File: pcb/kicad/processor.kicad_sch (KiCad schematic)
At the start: 1 part, among them U3 STM32F401RBTx

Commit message: Move USB to own sheet.
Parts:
- added C4 (x5): 100n, Capacitor_SMD:C_0805_2012Metric, symbol Device:C
- added C4 (x2): 4.7u, Capacitor_SMD:C_0805_2012Metric, symbol Device:C
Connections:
- net VDD: now reaches U3.1 (VBAT)
- net VDD: now also U3.19 (VDD), U3.32 (VDD), U3.48 (VDD), U3.64 (VDD), C4.1, C4.1, C4.1, C4.1, C4.1, C4.1
- net VCAP: now reaches U3.30 (VCAP1)
- net VCAP: now also C4.1
- new net GND: C4.2, C4.2, C4.2, C4.2, C4.2, C4.2, C4.2
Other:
- moved on the sheet: U3

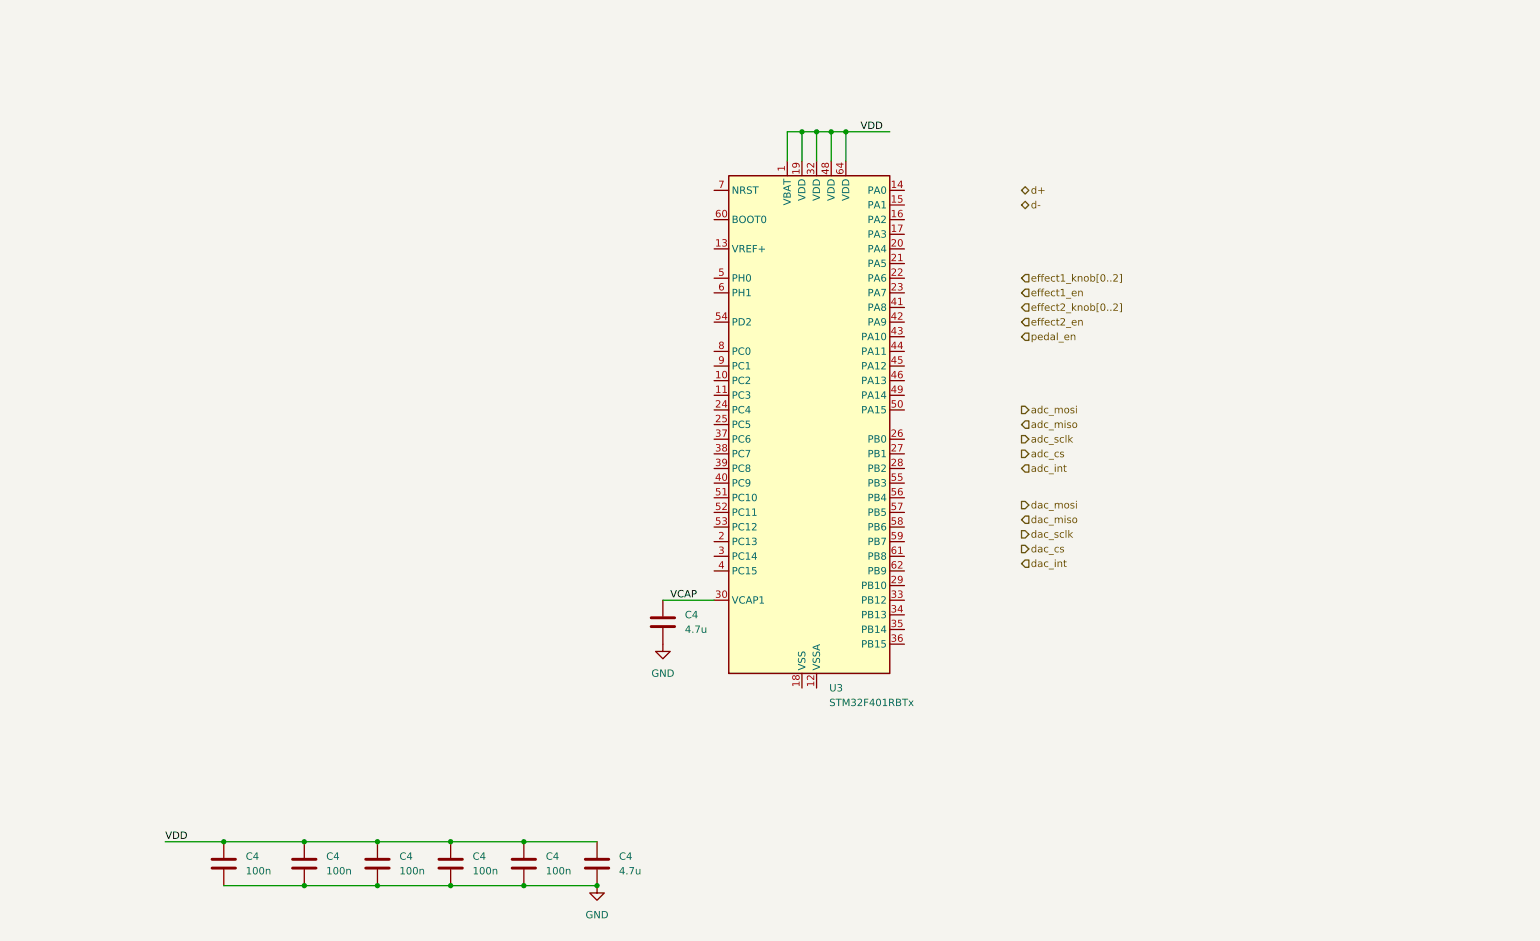
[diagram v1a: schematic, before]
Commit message: Add SoC and pinout.
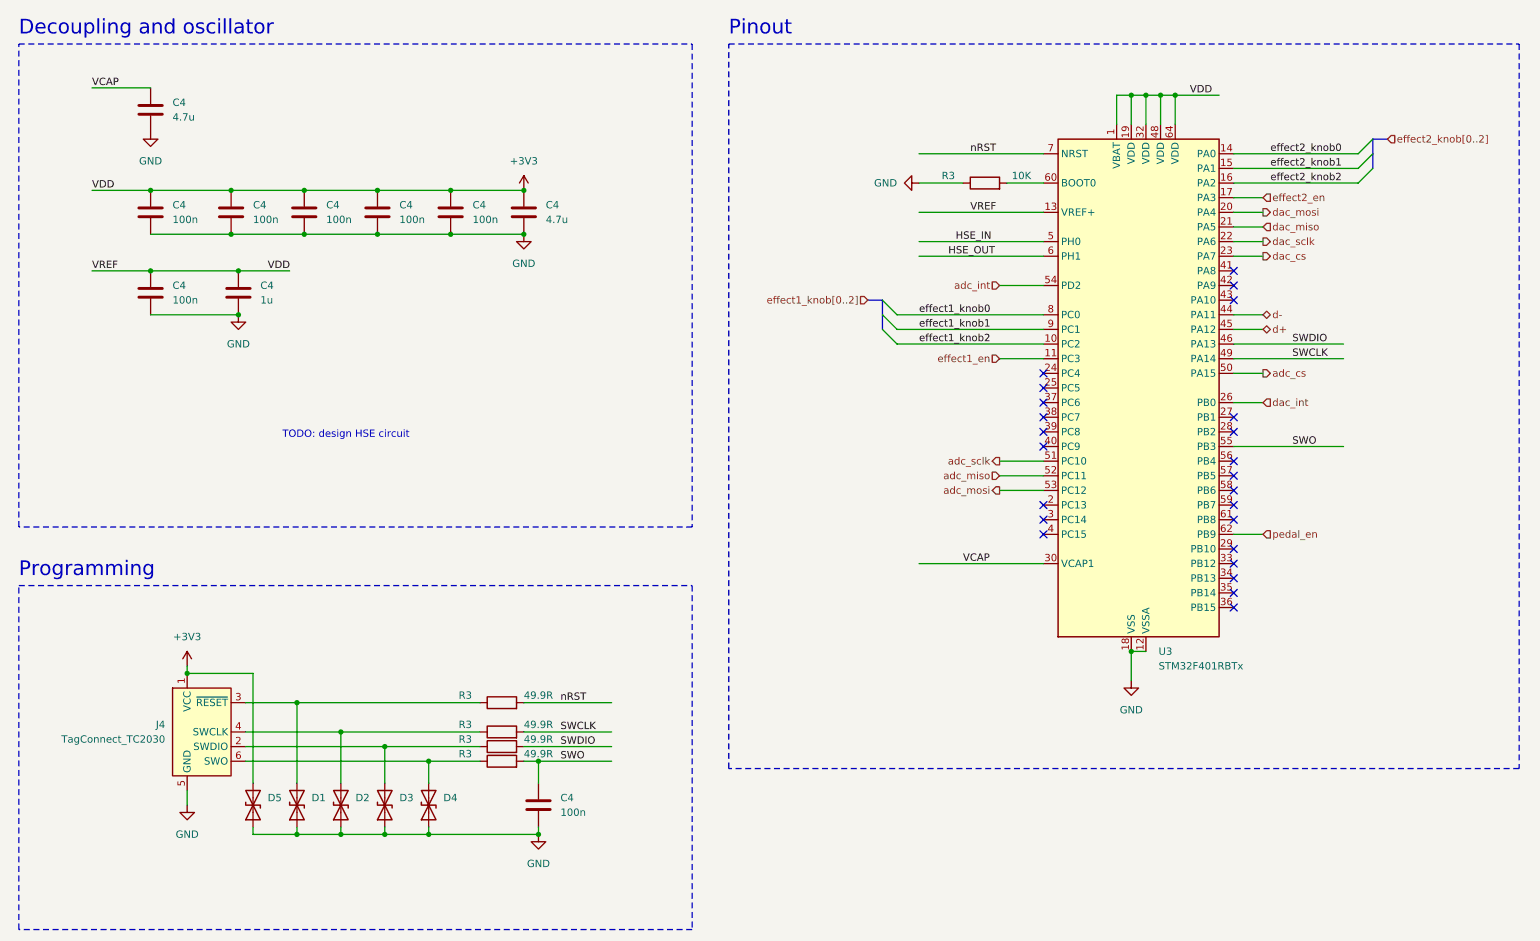
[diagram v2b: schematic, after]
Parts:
- removed C4: 4.7u, Capacitor_SMD:C_0805_2012Metric, symbol Device:C
- added C4: 1u, Capacitor_SMD:C_0805_2012Metric, symbol Device:C
- added C4 (x2): 100n, Capacitor_SMD:C_0805_2012Metric, symbol Device:C
- added C4: 4.7u, Capacitor_SMD:C_0805_2012Metric, symbol Device:C
- added D1, D2, D3, D4, D5: D_TVS, symbol Device:D_TVS
- added J4: TagConnect_TC2030, Connector:Tag-Connect_TC2030-IDC-FP_2x03_P1.27mm_Vertical, symbol Connector:Conn_ARM_SWD_TagConnect_TC2030
- added R3 (x4): 49.9R, Resistor_SMD:R_0805_2012Metric, symbol Device:R
- added R3: 10K, Resistor_SMD:R_0805_2012Metric, symbol Device:R
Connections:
- net VDD is gone; now on net +3V3: C4.1, C4.1, C4.1, C4.1, C4.1, C4.1, U3.1 (VBAT), U3.19 (VDD), U3.32 (VDD), U3.48 (VDD), U3.64 (VDD)
- net GND: now also U3.12 (VSSA), U3.18 (VSS), U3.31 (VSS), U3.47 (VSS), U3.63 (VSS), C4.2, C4.2, C4.2, C4.2, D1.1 (A1), D2.1 (A1), D3.1 (A1), D4.1 (A1), D5.1 (A1), J4.5 (GND), R3.1
- net VCAP: now also C4.1
- net adc_cs: now also U3.50 (PA15)
- net adc_int: now also U3.54 (PD2)
- net adc_miso: now also U3.52 (PC11)
- net adc_mosi: now also U3.53 (PC12)
- net adc_sclk: now also U3.51 (PC10)
- net d+: now also U3.45 (PA12)
- net d-: now also U3.44 (PA11)
- net dac_cs: now also U3.23 (PA7)
- net dac_int: now also U3.26 (PB0)
- net dac_miso: now also U3.21 (PA5)
- net dac_mosi: now also U3.20 (PA4)
- net dac_sclk: now also U3.22 (PA6)
- net effect1_en: now also U3.11 (PC3)
- net effect2_en: now also U3.17 (PA3)
- net pedal_en: now also U3.62 (PB9)
- net effect1_knob2: now reaches U3.10 (PC2)
- net +3V3: now reaches U3.13 (VREF+)
- net +3V3: now also C4.1, C4.1, D5.2 (A2), J4.1 (VCC)
- net effect2_knob0: now reaches U3.14 (PA0)
- net effect2_knob1: now reaches U3.15 (PA1)
- net effect2_knob2: now reaches U3.16 (PA2)
- net SWDIO: now reaches U3.46 (PA13)
- net SWDIO: now also R3.2
- net SWCLK: now reaches U3.49 (PA14)
- net SWCLK: now also R3.2
- net HSE_IN: now reaches U3.5 (PH0)
- net SWO: now reaches U3.55 (PB3)
- net SWO: now also C4.1, R3.2
- net HSE_OUT: now reaches U3.6 (PH1)
- net at U3.60 (BOOT0): now also R3.2
- net nRST: now reaches U3.7 (NRST)
- net nRST: now also R3.2
- net effect1_knob0: now reaches U3.8 (PC0)
- net effect1_knob1: now reaches U3.9 (PC1)
- new net: D4.2 (A2), J4.6 (SWO), R3.1
- new net: D3.2 (A2), J4.2 (SWDIO), R3.1
- new net: D1.2 (A2), J4.3 (~{RESET}), R3.1
- new net: D2.2 (A2), J4.4 (SWCLK), R3.1
- no-connect marks 0 -> 24
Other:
- note added: "Decoupling and oscillator"
- note added: "Pinout"
- note added: "Programming"
- note added: "TODO: design HSE circuit"
- moved on the sheet: C4, U3

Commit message: Add hse circuit.
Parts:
- added C4 (x2): 10p, Capacitor_SMD:C_0805_2012Metric, symbol Device:C
- added R3: 0R, Resistor_SMD:R_0805_2012Metric, symbol Device:R
- added Y1: 16MHz, symbol Device:Crystal_GND24
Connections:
- net GND: now also C4.2, C4.2, Y1.2, Y1.4
- net HSE_IN: now also C4.1, Y1.1
- net HSE_OUT: now also R3.2
- new net: C4.1, R3.1, Y1.3
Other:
- note added: "For RH100-16.000-8-2020-TR, C_0 = 8pF and ESR = 70R. Considering stray capacitance of 3 to 5pF, C_L = 2 * (C_0 - C_S) = 6 to 10pF."
- note removed: "TODO: design HSE circuit"

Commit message: Added converters, controls and updated annotations.
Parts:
- removed D1, D2, D3, D4, D5: D_TVS, symbol Device:D_TVS
- added D301, D302, D303, D304, D305: ~, symbol pedal-components:PESD3V3L1BA
- renumbered J4 to J301, U3 to U301, Y1 to Y301
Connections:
- net +3V3: now also D301.2 (A2)
- net GND: now also D301.1 (A1), D302.1 (A1), D303.1 (A1), D304.1 (A1), D305.1 (A1)
- net SWO: no longer C4.1
- net nRST: now also C4.1
- net DAC_NLDAC: now reaches U301.41 (PA8)
- net DAC_NCLR: now reaches U301.42 (PA9)
- net at J301.6 (SWO), R3.1: now also D305.2 (A2)
- net at J301.2 (SWDIO), R3.1: now also D304.2 (A2)
- net at J301.3 (~{RESET}), R3.1: now also D302.2 (A2)
- net at J301.4 (SWCLK), R3.1: now also D303.2 (A2)
- net adc_cs renamed ADC_NCS
- net adc_int: no longer names the net of U301.54 (PD2)
- net adc_miso renamed ADC_MISO
- net adc_mosi: no longer names the net of U301.53 (PC12)
- net adc_sclk renamed ADC_SCLK
- net d+ renamed D+
- net d- renamed D-
- net dac_cs renamed DAC_CS
- net dac_int: no longer names the net of U301.26 (PB0)
- net dac_miso: no longer names the net of U301.21 (PA5)
- net dac_mosi renamed DAC_MOSI
- net dac_sclk renamed DAC_SCLK
- net effect1_en renamed EFFECT1_EN
- net effect1_knob0 renamed EFFECT1_KNOB0
- net effect1_knob1 renamed EFFECT1_KNOB1
- net effect1_knob2 renamed EFFECT1_KNOB2
- net effect2_en renamed EFFECT2_EN
- net effect2_knob0 renamed EFFECT2_KNOB0
- net effect2_knob1 renamed EFFECT2_KNOB1
- net effect2_knob2 renamed EFFECT2_KNOB2
- net pedal_en renamed PEDAL_EN
- no-connect marks 24 -> 26
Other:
- moved on the sheet: C4, J301, R3

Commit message: Added PCB layout and fabrication output.
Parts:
- D301, D302, D303, D304, D305: footprint (none) -> pedal-components:PESD3V3L1BA
- Y301: footprint (none) -> pedal-components:RH100-16.000-8-2020-TR; Part Number (none) -> RH100-16.000-8-2020-TR; Part number RH100-16.000-8-2020-TR -> (none)
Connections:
- net TAG_SWO: now reaches D305.2 (A2), J301.6 (SWO), R3.1
- net HSE_PRE_OUT: now reaches C4.1, R3.1, Y301.3
- net TAG_SWDIO: now reaches D304.2 (A2), J301.2 (SWDIO), R3.1
- net BOOT0: now reaches R3.2, U301.60 (BOOT0)
- net TAG_nRST: now reaches D302.2 (A2), J301.3 (~{RESET}), R3.1
- net TAG_SWCLK: now reaches D303.2 (A2), J301.4 (SWCLK), R3.1
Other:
- moved on the sheet: R3

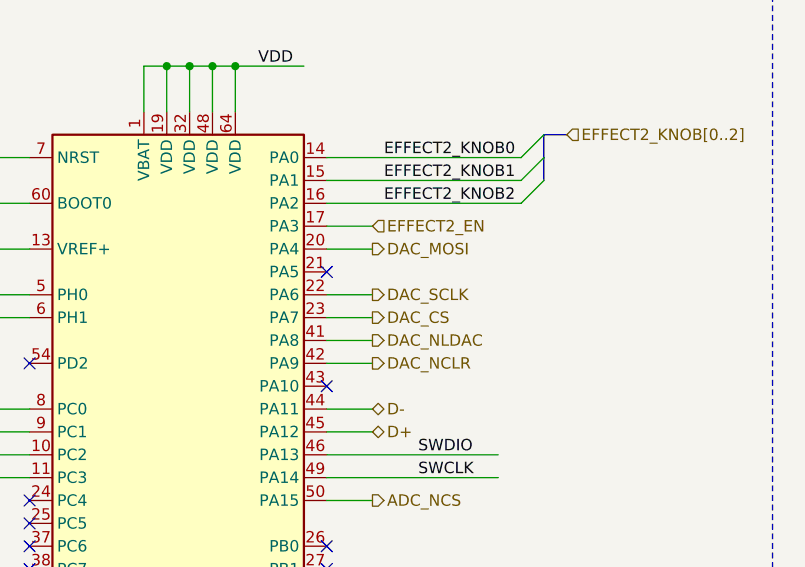
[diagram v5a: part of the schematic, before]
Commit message: Update .ioc file and fix DAC pinout.
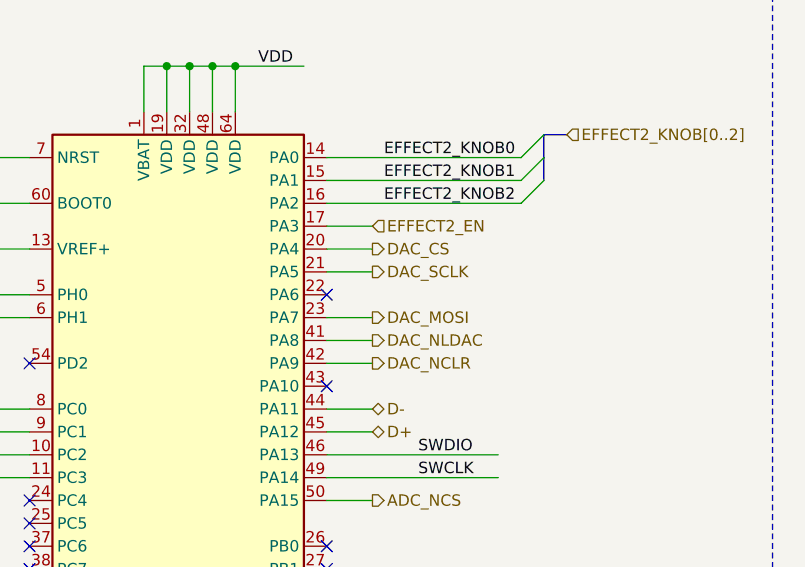
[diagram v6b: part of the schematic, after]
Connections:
- net DAC_CS: now also U301.20 (PA4); no longer U301.23 (PA7)
- net DAC_MOSI: now also U301.23 (PA7); no longer U301.20 (PA4)
- net DAC_SCLK: now also U301.21 (PA5); no longer U301.22 (PA6)
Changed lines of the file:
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@@
   (no_connect (at 198.12 99.06))
   (no_connect (at 198.12 73.66))
-  (no_connect (at 231.14 63.5))
   (no_connect (at 198.12 91.44))
   (no_connect (at 231.14 99.06))
@@
   (no_connect (at 231.14 121.92))
   (no_connect (at 231.14 104.14))
+  (no_connect (at 231.14 66.04))
   (no_connect (at 231.14 76.2))
   (bus_entry (at 255.27 50.8) (size -2.54 2.54)
@@
     (stroke (width 0) (type default))
   )
-  (wire (pts (xy 231.14 66.04) (xy 236.22 66.04))
-    (stroke (width 0) (type default))
-  )
   (wire (pts (xy 58.42 71.12) (xy 67.31 71.12))
     (stroke (width 0) (type default))
@@
   )
   (wire (pts (xy 71.12 168.91) (xy 71.12 167.64))
+    (stroke (width 0) (type default))
+  )
+  (wire (pts (xy 231.14 63.5) (xy 236.22 63.5))
     (stroke (width 0) (type default))
   )
@@
     (effects (font (size 1.27 1.27)) (justify left bottom))
   )
+  (hierarchical_label "DAC_MOSI" (shape output) (at 236.22 68.58 0) (fields_autoplaced)
+    (effects (font (size 1.27 1.27)) (justify left))
+  )
   (hierarchical_label "D-" (shape bidirectional) (at 236.22 78.74 0) (fields_autoplaced)
     (effects (font (size 1.27 1.27)) (justify left))
@@
     (effects (font (size 1.27 1.27)) (justify right))
   )
-  (hierarchical_label "DAC_CS" (shape output) (at 236.22 68.58 0) (fields_autoplaced)
-    (effects (font (size 1.27 1.27)) (justify left))
-  )
   (hierarchical_label "EFFECT1_KNOB[0..2]" (shape input) (at 167.64 76.2 180) (fields_autoplaced)
     (effects (font (size 1.27 1.27)) (justify right))
   )
+  (hierarchical_label "DAC_CS" (shape output) (at 236.22 60.96 0) (fields_autoplaced)
+    (effects (font (size 1.27 1.27)) (justify left))
+  )
   (hierarchical_label "ADC_NCS" (shape output) (at 236.22 88.9 0) (fields_autoplaced)
     (effects (font (size 1.27 1.27)) (justify left))
   )
   (hierarchical_label "DAC_NLDAC" (shape output) (at 236.22 71.12 0) (fields_autoplaced)
-    (effects (font (size 1.27 1.27)) (justify left))
-  )
-  (hierarchical_label "DAC_SCLK" (shape output) (at 236.22 66.04 0) (fields_autoplaced)
     (effects (font (size 1.27 1.27)) (justify left))
   )
@@
     (effects (font (size 1.27 1.27)) (justify right))
   )
-  (hierarchical_label "DAC_MOSI" (shape output) (at 236.22 60.96 0) (fields_autoplaced)
-    (effects (font (size 1.27 1.27)) (justify left))
-  )
+  (hierarchical_label "DAC_SCLK" (shape output) (at 236.22 63.5 0) (fields_autoplaced)
+    (effects (font (size 1.27 1.27)) (justify left))
+  )
